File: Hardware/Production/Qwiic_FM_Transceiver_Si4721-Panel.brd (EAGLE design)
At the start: 54.6 x 34.3 mm, 60 parts, among them J1 AUDIO_JACK_3.5MM_SMD, J2 AUDIO_JACK_3.5MM_SMD, J4 QWIIC_RIGHT_ANGLE, J5 QWIIC_RIGHT_ANGLE, U1 SI4721, U3 TPA6111A2DR, Y1 32.768kHz

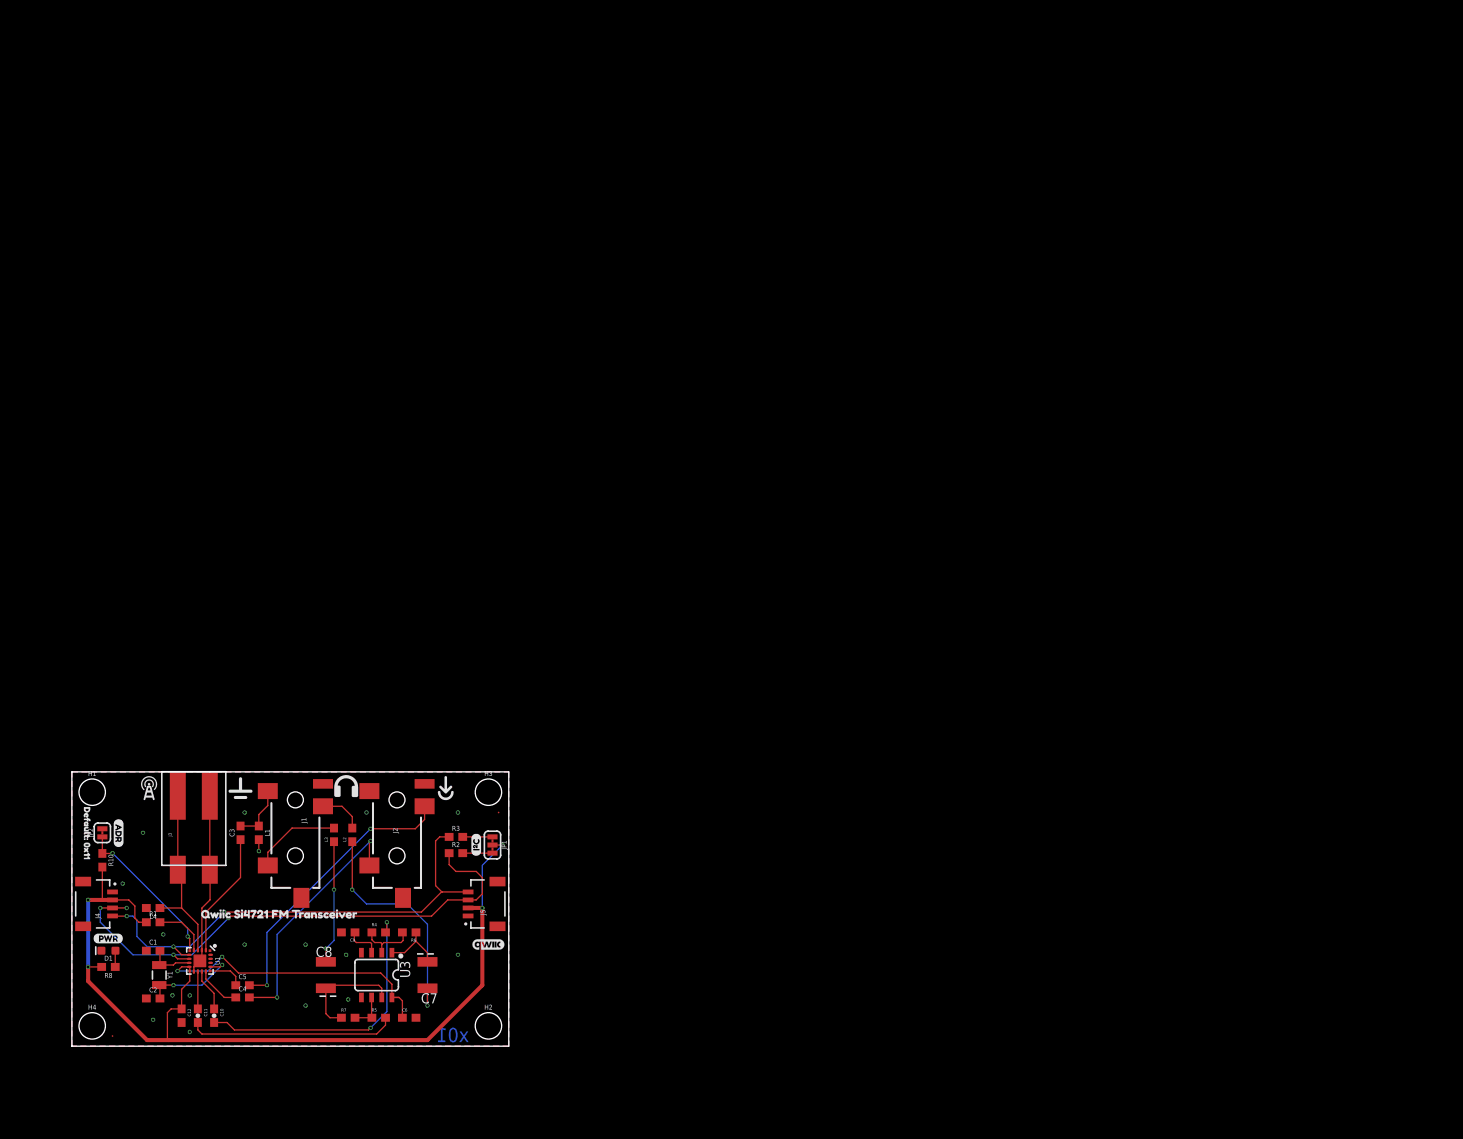
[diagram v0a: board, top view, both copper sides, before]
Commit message: x01 protos ordered
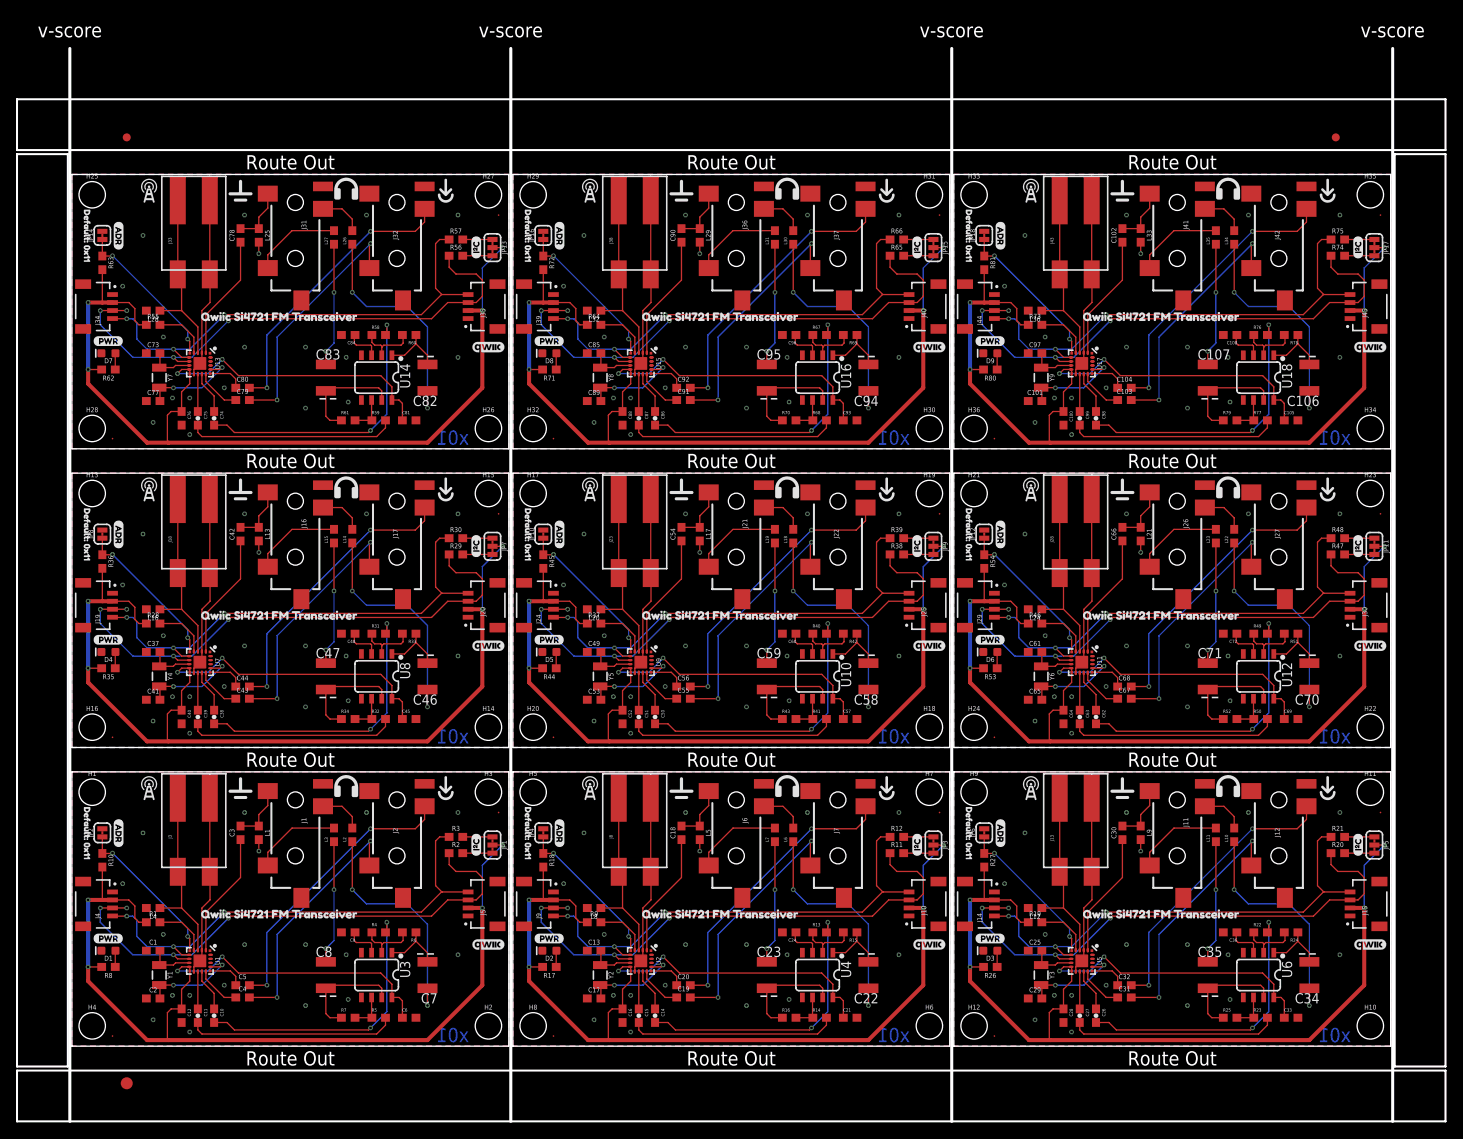
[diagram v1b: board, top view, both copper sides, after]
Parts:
- removed FRAME1: FRAME-LETTER, SparkFun-Aesthetics:CREATIVE_COMMONS
- added C100, C16, C28, C40, C52, C64, C76, C88: 22nF, SparkFun-Capacitors:0603
- added C101, C13, C17, C25, C29, C37, C41, C49, C53, C61, C65, C73, C77, C85, C89, C97: 15pF, SparkFun-Capacitors:0603
- added C102, C18, C30, C42, C54, C66, C78, C90: 1nF, SparkFun-Capacitors:0603
- added C103, C104, C19, C20, C31, C32, C43, C44, C55, C56, C67, C68, C79, C80, C91, C92: 0.47uF, SparkFun-Capacitors:0603
- added C105, C108, C21, C24, C33, C36, C45, C48, C57, C60, C69, C72, C81, C84, C93, C96: 0.1uF, SparkFun-Capacitors:0603
- added C106, C107, C22, C23, C34, C35, C46, C47, C58, C59, C70, C71, C82, C83, C94, C95: 47uF, SparkFun-Capacitors:EIA3528
- added C14, C15, C26, C27, C38, C39, C50, C51, C62, C63, C74, C75, C86, C87, C98, C99: 1uF, SparkFun-Capacitors:0603-CAP
- added D2, D3, D4, D5, D6, D7, D8, D9: RED, SparkFun-LED:LED-0603
- added E$1, E$2: (no value), SparkFun-Aesthetics:FIDUCIAL-1X2
- added E$3: (no value), SparkFun-Retired:FIDUCIAL-1.5X3
- added FD10, FD11, FD12, FD13, FD14, FD15, FD16, FD17, FD18, FD3, FD4, FD5, FD6, FD7, FD8, FD9: FIDUCIAL0.2MM, SparkFun-Aesthetics:FIDUCIAL-0.2MM
- added H10, H11, H12, H13, H14, H15, H16, H17, H18, H19, H20, H21, H22, H23, H24, H25, H26, H27, H28, H29, H30, H31, H32, H33, H34, H35, H36, H5, H6, H7, H8, H9: STAND-OFF, SparkFun-Hardware:STAND-OFF
- added J10, J14, J15, J19, J20, J24, J25, J29, J30, J34, J35, J39, J40, J44, J45, J9: QWIIC_RIGHT_ANGLE, SparkFun-Connectors:JST04_1MM_RA
- added J11, J12, J16, J17, J21, J22, J26, J27, J31, J32, J36, J37, J41, J42, J6, J7: AUDIO_JACK_3.5MM_SMD, SparkFun-Connectors:AUDIO-JACK-3.5MM-SMD
- added J13, J18, J23, J28, J33, J38, J43, J8: (no value), SparkFun-Connectors:1X02_POKEHOME
- added JP10, JP12, JP14, JP16, JP18, JP4, JP6, JP8: (no value), SparkFun-Jumpers:SMT-JUMPER_2_NC_TRACE_SILK
- added JP11, JP13, JP15, JP17, JP3, JP5, JP7, JP9: JUMPER-SMT_3_2-NC_TRACE_SILK, SparkFun-Jumpers:SMT-JUMPER_3_2-NC_TRACE_SILK
- added L10, L14, L18, L22, L26, L30, L34, L6: FERITE 2.5k, SparkFun-Coils:0603
- added L11, L15, L19, L23, L27, L31, L35, L7: FERITE 2.5K, SparkFun-Coils:0603
- added L12, L16, L20, L24, L28, L32, L36, L8: 120nH, SparkFun-Coils:0603
- added L13, L17, L21, L25, L29, L33, L5, L9: 270nH, SparkFun-Coils:0603
- added R11, R12, R20, R21, R29, R30, R38, R39, R47, R48, R56, R57, R65, R66, R74, R75: 2.2k, SparkFun-Resistors:0603
- added R13, R14, R15, R16, R22, R23, R24, R25, R31, R32, R33, R34, R40, R41, R42, R43, R49, R50, R51, R52, R58, R59, R60, R61, R67, R68, R69, R70, R76, R77, R78, R79: 20k, SparkFun-Resistors:0603
- added R17, R26, R35, R44, R53, R62, R71, R80: 1k, SparkFun-Resistors:0603
- added R18, R27, R36, R45, R54, R63, R72, R81: 100k, SparkFun-Resistors:0603
- added R19, R28, R37, R46, R55, R64, R73, R9: 10k, SparkFun-Resistors:0603
- added U$100, U$117, U$134, U$151, U$32, U$49, U$66, U$83: (no value), Labels:PWR-()-03
- added U$101, U$118, U$135, U$152, U$33, U$50, U$67, U$84: (no value), Labels:I_SUPER2_C-()-03
- added U$102, U$119, U$136, U$153, U$34, U$51, U$68, U$85: (no value), Labels:ADR-()-03
- added U$103, U$115, U$120, U$132, U$137, U$149, U$17, U$30, U$35, U$47, U$52, U$64, U$69, U$81, U$86, U$98: (no value), si4721label:QWIIC_SI4721_FM_TRANSCEIVER0
- added U$104, U$121, U$138, U$19, U$36, U$53, U$70, U$87: (no value), SparkFun-Aesthetics:QWIIC_4MM
- added U$105, U$122, U$139, U$20, U$37, U$54, U$71, U$88: (no value), SparkFun-Aesthetics:OSHW-LOGO-S
- added U$106, U$123, U$140, U$21, U$38, U$55, U$72, U$89: (no value), si4721connlabels:ANTENNA1
- added U$107, U$124, U$141, U$22, U$39, U$56, U$73, U$90: (no value), si4721connlabels:GND0
- added U$108, U$125, U$142, U$23, U$40, U$57, U$74, U$91: (no value), si4721connlabels:LINE_IN2
- added U$109, U$126, U$143, U$24, U$41, U$58, U$75, U$92: (no value), si4721connlabels:PHONES_OUT3
- added U$110, U$127, U$144, U$25, U$42, U$59, U$76, U$93: (no value), phones#png:PHONES#PNG
- added U$111, U$128, U$145, U$26, U$43, U$60, U$77, U$94: (no value), in#png:IN#PNG
- added U$112, U$129, U$146, U$27, U$44, U$61, U$78, U$95: (no value), gnd#png:GND#PNG
- added U$113, U$130, U$147, U$28, U$45, U$62, U$79, U$96: (no value), antenna#png:ANTENNA#PNG
- added U$114, U$131, U$148, U$29, U$46, U$63, U$80, U$97: SPARKX-LOGO4, SparkX:SPARKX-MEDIUM
- added U$116, U$133, U$150, U$31, U$48, U$65, U$82, U$99: (no value), defaultadr:DEFAULT#_0X110
- added U10, U12, U14, U16, U18, U4, U6, U8: TPA6111A2DR, SparkFun-IC-Amplifiers:SO08
- added U11, U13, U15, U17, U2, U5, U7, U9: SI4721, SparkFun-RF:QFN-20-3X3MM
- added Y2, Y3, Y4, Y5, Y6, Y7, Y8, Y9: 32.768kHz, SparkFun-Clocks:CRYSTAL-SMD-3.2X1.5MM
- moved J3 0.25 mm to (15.2, 27.1)
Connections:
- new net 3.3V1: C16.1, C21.1, J10.2, J9.2, JP3.2, R17.2, R18.2, R9.1, U2.10, U2.11, U4.8
- new net 3.3V2: C28.1, C33.1, J14.2, J15.2, JP5.2, R19.1, R26.2, R27.2, U5.10, U5.11, U6.8
- new net 3.3V3: C40.1, C45.1, J19.2, J20.2, JP7.2, R28.1, R35.2, R36.2, U7.10, U7.11, U8.8
- new net 3.3V4: C52.1, C57.1, J24.2, J25.2, JP9.2, R37.1, R44.2, R45.2, U10.8, U9.10, U9.11
- new net 3.3V5: C64.1, C69.1, J29.2, J30.2, JP11.2, R46.1, R53.2, R54.2, U11.10, U11.11, U12.8
- new net 3.3V6: C76.1, C81.1, J34.2, J35.2, JP13.2, R55.1, R62.2, R63.2, U13.10, U13.11, U14.8
- new net 3.3V7: C88.1, C93.1, J39.2, J40.2, JP15.2, R64.1, R71.2, R72.2, U15.10, U15.11, U16.8
- new net 3.3V8: C100.1, C105.1, J44.2, J45.2, JP17.2, R73.1, R80.2, R81.2, U17.10, U17.11, U18.8
- new net ADDR1: JP4.1, R18.1, U2.6
- new net ADDR2: JP6.1, R27.1, U5.6
- new net ADDR3: JP8.1, R36.1, U7.6
- new net ADDR4: JP10.1, R45.1, U9.6
- new net ADDR5: JP12.1, R54.1, U11.6
- new net ADDR6: JP14.1, R63.1, U13.6
- new net ADDR7: JP16.1, R72.1, U15.6
- new net ADDR8: JP18.1, R81.1, U17.6
- new net FMI1: C18.1, U2.2
- new net FMI2: C30.1, U5.2
- new net FMI3: C42.1, U7.2
- new net FMI4: C54.1, U9.2
- new net FMI5: C66.1, U11.2
- new net FMI6: C78.1, U13.2
- new net FMI7: C90.1, U15.2
- new net FMI8: C102.1, U17.2
- new net GND1: C13.1, C16.2, C17.1, C21.2, C24.2, D2.C, J10.1, J7.SLEEVE, J8.P1, J8.P3, J9.1, JP4.2, L5.2, L8.2, U2.12, U2.21, U2.3, U4.4, U4.5
- new net GND2: C25.1, C28.2, C29.1, C33.2, C36.2, D3.C, J12.SLEEVE, J13.P1, J13.P3, J14.1, J15.1, JP6.2, L12.2, L9.2, U5.12, U5.21, U5.3, U6.4, U6.5
- new net GND3: C37.1, C40.2, C41.1, C45.2, C48.2, D4.C, J17.SLEEVE, J18.P1, J18.P3, J19.1, J20.1, JP8.2, L13.2, L16.2, U7.12, U7.21, U7.3, U8.4, U8.5
- new net GND4: C49.1, C52.2, C53.1, C57.2, C60.2, D5.C, J22.SLEEVE, J23.P1, J23.P3, J24.1, J25.1, JP10.2, L17.2, L20.2, U10.4, U10.5, U9.12, U9.21, U9.3
- new net GND5: C61.1, C64.2, C65.1, C69.2, C72.2, D6.C, J27.SLEEVE, J28.P1, J28.P3, J29.1, J30.1, JP12.2, L21.2, L24.2, U11.12, U11.21, U11.3, U12.4, U12.5
- new net GND6: C73.1, C76.2, C77.1, C81.2, C84.2, D7.C, J32.SLEEVE, J33.P1, J33.P3, J34.1, J35.1, JP14.2, L25.2, L28.2, U13.12, U13.21, U13.3, U14.4, U14.5
- new net GND7: C85.1, C88.2, C89.1, C93.2, C96.2, D8.C, J37.SLEEVE, J38.P1, J38.P3, J39.1, J40.1, JP16.2, L29.2, L32.2, U15.12, U15.21, U15.3, U16.4, U16.5
- new net GND8: C100.2, C101.1, C105.2, C108.2, C97.1, D9.C, J42.SLEEVE, J43.P1, J43.P3, J44.1, J45.1, JP18.2, L33.2, L36.2, U17.12, U17.21, U17.3, U18.4, U18.5
- new net GPO10: U9.18
- new net GPO11: U11.19
- new net GPO12: U11.18
- new net GPO13: U13.19
- new net GPO14: U13.18
- new net GPO15: U15.19
- new net GPO16: U15.18
- new net GPO17: U17.19
- new net GPO18: U17.18
- new net GPO3: U2.19
- new net GPO4: U2.18
- new net GPO5: U5.19
- new net GPO6: U5.18
- new net GPO7: U7.19
- new net GPO8: U7.18
- new net GPO9: U9.19
- new net LIN1: C20.1, U2.16
- new net LIN2: C32.1, U5.16
- new net LIN3: C44.1, U7.16
- new net LIN4: C56.1, U9.16
- new net LIN5: C68.1, U11.16
- new net LIN6: C80.1, U13.16
- new net LIN7: C92.1, U15.16
- new net LIN8: C104.1, U17.16
- new net LOUT1: C14.1, U2.14
- new net LOUT2: C26.1, U5.14
- new net LOUT3: C38.1, U7.14
- new net LOUT4: C50.1, U9.14
- new net LOUT5: C62.1, U11.14
- new net LOUT6: C74.1, U13.14
- new net LOUT7: C86.1, U15.14
- new net LOUT8: C98.1, U17.14
- new net N$100: D5.A, R44.1
- new net N$101: C61.2, U11.9, Y6.P$1
- new net N$102: C65.2, U11.17, Y6.P$2
- new net N$103: R46.2, U11.5
- new net N$104: C66.2, J26.SLEEVE, L21.1
- new net N$105: C70.A, R51.1, U12.1
- new net N$106: C71.A, R52.1, U12.7
- new net N$107: C72.1, U12.3
- new net N$108: R49.1, R51.2, U12.2
- new net N$109: R50.1, R52.2, U12.6
- new net N$110: C62.2, R49.2
- new net N$111: C63.2, R50.2
- new net N$112: C70.C, L22.1
- new net N$113: C71.C, L23.1
- new net N$114: J26.RING, L22.2
- new net N$115: J26.TIP, L23.2
- new net N$116: C67.2, J27.TIP
- new net N$117: C68.2, J27.RING
- new net N$118: JP11.3, R47.2
- new net N$119: JP11.1, R48.2
- new net N$120: D6.A, R53.1
- new net N$121: C73.2, U13.9, Y7.P$1
- new net N$122: C77.2, U13.17, Y7.P$2
- new net N$123: R55.2, U13.5
- new net N$124: C78.2, J31.SLEEVE, L25.1
- new net N$125: C82.A, R60.1, U14.1
- new net N$126: C83.A, R61.1, U14.7
- new net N$127: C84.1, U14.3
- new net N$128: R58.1, R60.2, U14.2
- new net N$129: R59.1, R61.2, U14.6
- new net N$130: C74.2, R58.2
- new net N$131: C75.2, R59.2
- new net N$132: C82.C, L26.1
- new net N$133: C83.C, L27.1
- new net N$134: J31.RING, L26.2
- new net N$135: J31.TIP, L27.2
- new net N$136: C79.2, J32.TIP
- new net N$137: C80.2, J32.RING
- new net N$138: JP13.3, R56.2
- new net N$139: JP13.1, R57.2
- new net N$140: D7.A, R62.1
- new net N$141: C85.2, U15.9, Y8.P$1
- new net N$142: C89.2, U15.17, Y8.P$2
- new net N$143: R64.2, U15.5
- new net N$144: C90.2, J36.SLEEVE, L29.1
- new net N$145: C94.A, R69.1, U16.1
- new net N$146: C95.A, R70.1, U16.7
- new net N$147: C96.1, U16.3
- new net N$148: R67.1, R69.2, U16.2
- new net N$149: R68.1, R70.2, U16.6
- new net N$150: C86.2, R67.2
- new net N$151: C87.2, R68.2
- new net N$152: C94.C, L30.1
- new net N$153: C95.C, L31.1
- new net N$154: J36.RING, L30.2
- new net N$155: J36.TIP, L31.2
- new net N$156: C91.2, J37.TIP
- new net N$157: C92.2, J37.RING
- new net N$158: JP15.3, R65.2
- new net N$159: JP15.1, R66.2
- new net N$160: D8.A, R71.1
- new net N$161: C97.2, U17.9, Y9.P$1
- new net N$162: C101.2, U17.17, Y9.P$2
- new net N$163: R73.2, U17.5
- new net N$164: C102.2, J41.SLEEVE, L33.1
- new net N$165: C106.A, R78.1, U18.1
- new net N$166: C107.A, R79.1, U18.7
- new net N$167: C108.1, U18.3
- new net N$168: R76.1, R78.2, U18.2
- new net N$169: R77.1, R79.2, U18.6
- new net N$170: C98.2, R76.2
- new net N$171: C99.2, R77.2
- new net N$172: C106.C, L34.1
- new net N$173: C107.C, L35.1
- new net N$174: J41.RING, L34.2
- new net N$175: J41.TIP, L35.2
- new net N$176: C103.2, J42.TIP
- new net N$177: C104.2, J42.RING
- new net N$178: JP17.3, R74.2
- new net N$179: JP17.1, R75.2
- new net N$180: D9.A, R80.1
- new net N$21: C13.2, U2.9, Y2.P$1
- new net N$22: C17.2, U2.17, Y2.P$2
- new net N$23: R9.2, U2.5
- new net N$24: C18.2, J6.SLEEVE, L5.1
- new net N$25: C22.A, R15.1, U4.1
- new net N$26: C23.A, R16.1, U4.7
- new net N$27: C24.1, U4.3
- new net N$28: R13.1, R15.2, U4.2
- new net N$29: R14.1, R16.2, U4.6
- new net N$30: C14.2, R13.2
- new net N$31: C15.2, R14.2
- new net N$32: C22.C, L6.1
- new net N$33: C23.C, L7.1
- new net N$34: J6.RING, L6.2
- new net N$35: J6.TIP, L7.2
- new net N$36: C19.2, J7.TIP
- new net N$37: C20.2, J7.RING
- new net N$38: JP3.3, R11.2
- new net N$39: JP3.1, R12.2
- new net N$40: D2.A, R17.1
- new net N$41: C25.2, U5.9, Y3.P$1
- new net N$42: C29.2, U5.17, Y3.P$2
- new net N$43: R19.2, U5.5
- new net N$44: C30.2, J11.SLEEVE, L9.1
- new net N$45: C34.A, R24.1, U6.1
- new net N$46: C35.A, R25.1, U6.7
- new net N$47: C36.1, U6.3
- new net N$48: R22.1, R24.2, U6.2
- new net N$49: R23.1, R25.2, U6.6
- new net N$50: C26.2, R22.2
- new net N$51: C27.2, R23.2
- new net N$52: C34.C, L10.1
- new net N$53: C35.C, L11.1
- new net N$54: J11.RING, L10.2
- new net N$55: J11.TIP, L11.2
- new net N$56: C31.2, J12.TIP
- new net N$57: C32.2, J12.RING
- new net N$58: JP5.3, R20.2
- new net N$59: JP5.1, R21.2
- new net N$60: D3.A, R26.1
- new net N$61: C37.2, U7.9, Y4.P$1
- new net N$62: C41.2, U7.17, Y4.P$2
- new net N$63: R28.2, U7.5
- new net N$64: C42.2, J16.SLEEVE, L13.1
- new net N$65: C46.A, R33.1, U8.1
- new net N$66: C47.A, R34.1, U8.7
- new net N$67: C48.1, U8.3
- new net N$68: R31.1, R33.2, U8.2
- new net N$69: R32.1, R34.2, U8.6
- new net N$70: C38.2, R31.2
- new net N$71: C39.2, R32.2
- new net N$72: C46.C, L14.1
- new net N$73: C47.C, L15.1
- new net N$74: J16.RING, L14.2
- new net N$75: J16.TIP, L15.2
- new net N$76: C43.2, J17.TIP
- new net N$77: C44.2, J17.RING
- new net N$78: JP7.3, R29.2
- new net N$79: JP7.1, R30.2
- new net N$80: D4.A, R35.1
- new net N$81: C49.2, U9.9, Y5.P$1
- new net N$82: C53.2, U9.17, Y5.P$2
- new net N$83: R37.2, U9.5
- new net N$84: C54.2, J21.SLEEVE, L17.1
- new net N$85: C58.A, R42.1, U10.1
- new net N$86: C59.A, R43.1, U10.7
- new net N$87: C60.1, U10.3
- new net N$88: R40.1, R42.2, U10.2
- new net N$89: R41.1, R43.2, U10.6
- new net N$90: C50.2, R40.2
- new net N$91: C51.2, R41.2
- new net N$92: C58.C, L18.1
- new net N$93: C59.C, L19.1
- new net N$94: J21.RING, L18.2
- new net N$95: J21.TIP, L19.2
- new net N$96: C55.2, J22.TIP
- new net N$97: C56.2, J22.RING
- new net N$98: JP9.3, R38.2
- new net N$99: JP9.1, R39.2
- new net RIN1: C19.1, U2.15
- new net RIN2: C31.1, U5.15
- new net RIN3: C43.1, U7.15
- new net RIN4: C55.1, U9.15
- new net RIN5: C67.1, U11.15
- new net RIN6: C79.1, U13.15
- new net RIN7: C91.1, U15.15
- new net RIN8: C103.1, U17.15
- new net ROUT1: C15.1, U2.13
- new net ROUT2: C27.1, U5.13
- new net ROUT3: C39.1, U7.13
- new net ROUT4: C51.1, U9.13
- new net ROUT5: C63.1, U11.13
- new net ROUT6: C75.1, U13.13
- new net ROUT7: C87.1, U15.13
- new net ROUT8: C99.1, U17.13
- new net SCLK1: J10.4, J9.4, R12.1, U2.7
- new net SCLK2: J14.4, J15.4, R21.1, U5.7
- new net SCLK3: J19.4, J20.4, R30.1, U7.7
- new net SCLK4: J24.4, J25.4, R39.1, U9.7
- new net SCLK5: J29.4, J30.4, R48.1, U11.7
- new net SCLK6: J34.4, J35.4, R57.1, U13.7
- new net SCLK7: J39.4, J40.4, R66.1, U15.7
- new net SCLK8: J44.4, J45.4, R75.1, U17.7
- new net SDIO1: J10.3, J9.3, R11.1, U2.8
- new net SDIO2: J14.3, J15.3, R20.1, U5.8
- new net SDIO3: J19.3, J20.3, R29.1, U7.8
- new net SDIO4: J24.3, J25.3, R38.1, U9.8
- new net SDIO5: J29.3, J30.3, R47.1, U11.8
- new net SDIO6: J34.3, J35.3, R56.1, U13.8
- new net SDIO7: J39.3, J40.3, R65.1, U15.8
- new net SDIO8: J44.3, J45.3, R74.1, U17.8
- new net TXO1: J8.P2, J8.P4, L8.1, U2.4
- new net TXO2: J13.P2, J13.P4, L12.1, U5.4
- new net TXO3: J18.P2, J18.P4, L16.1, U7.4
- new net TXO4: J23.P2, J23.P4, L20.1, U9.4
- new net TXO5: J28.P2, J28.P4, L24.1, U11.4
- new net TXO6: J33.P2, J33.P4, L28.1, U13.4
- new net TXO7: J38.P2, J38.P4, L32.1, U15.4
- new net TXO8: J43.P2, J43.P4, L36.1, U17.4
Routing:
- net 3.3V4: track 0.00 -> 149.1 mm, vias 0 -> 6
- net 3.3V3: track 0.00 -> 149.1 mm, vias 0 -> 6
- net 3.3V8: track 0.00 -> 149.1 mm, vias 0 -> 6
- net 3.3V5: track 0.00 -> 149.1 mm, vias 0 -> 6
- net 3.3V2: track 0.00 -> 149.1 mm, vias 0 -> 6
- net 3.3V7: track 0.00 -> 149.1 mm, vias 0 -> 6
- net 3.3V6: track 0.00 -> 149.1 mm, vias 0 -> 6
- net 3.3V1: track 0.00 -> 149.1 mm, vias 0 -> 6
- net SDIO8: track 0.00 -> 68.1 mm, vias 0 -> 4
- net SDIO5: track 0.00 -> 68.1 mm, vias 0 -> 4
- net SDIO2: track 0.00 -> 68.1 mm, vias 0 -> 4
- net SDIO7: track 0.00 -> 68.1 mm, vias 0 -> 4
- net SDIO4: track 0.00 -> 68.1 mm, vias 0 -> 4
- net SDIO3: track 0.00 -> 68.1 mm, vias 0 -> 4
- net SDIO1: track 0.00 -> 68.1 mm, vias 0 -> 4
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- added copper zone on layer 1, net GND1
- added copper zone on layer 16, net GND1
- added copper zone on layer 1, net GND2
- added copper zone on layer 16, net GND2
- added copper zone on layer 1, net GND3
- added copper zone on layer 16, net GND3
- added copper zone on layer 1, net GND4
- added copper zone on layer 16, net GND4
- added copper zone on layer 1, net GND5
- added copper zone on layer 16, net GND5
- added copper zone on layer 1, net GND6
- added copper zone on layer 16, net GND6
- added copper zone on layer 1, net GND7
- added copper zone on layer 16, net GND7
- added copper zone on layer 1, net GND8
- added copper zone on layer 16, net GND8
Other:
- board size 54.6 x 34.3 mm -> 178.6 x 134.1 mm
- board text added: "Route Out"
- board text added: "v-score"

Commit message: x02 hardware order
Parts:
- removed C100, C88: 22nF, SparkFun-Capacitors:0603
- removed C101, C85, C89, C97: 15pF, SparkFun-Capacitors:0603
- removed C102, C90: 1nF, SparkFun-Capacitors:0603
- removed C103, C104, C79, C80, C91, C92: 0.47uF, SparkFun-Capacitors:0603
- removed C105, C108, C81, C84, C93, C96: 0.1uF, SparkFun-Capacitors:0603
- removed C106, C107, C82, C83, C94, C95: 47uF, SparkFun-Capacitors:EIA3528
- removed C86, C87, C98, C99: 1uF, SparkFun-Capacitors:0603-CAP
- removed D7, D8, D9: RED, SparkFun-LED:LED-0603
- removed FD13, FD14, FD15, FD16, FD17, FD18: FIDUCIAL0.2MM, SparkFun-Aesthetics:FIDUCIAL-0.2MM
- removed H25, H26, H27, H28, H29, H30, H31, H32, H33, H34, H35, H36: STAND-OFF, SparkFun-Hardware:STAND-OFF
- removed J31, J32, J36, J37, J41, J42: AUDIO_JACK_3.5MM_SMD, SparkFun-Connectors:AUDIO-JACK-3.5MM-SMD
- removed J33, J38, J43: (no value), SparkFun-Connectors:1X02_POKEHOME
- removed J34, J35, J39, J40, J44, J45: QWIIC_RIGHT_ANGLE, SparkFun-Connectors:JST04_1MM_RA
- removed JP13, JP15, JP17: JUMPER-SMT_3_2-NC_TRACE_SILK, SparkFun-Jumpers:SMT-JUMPER_3_2-NC_TRACE_SILK
- removed JP14, JP16, JP18: (no value), SparkFun-Jumpers:SMT-JUMPER_2_NC_TRACE_SILK
- removed L25, L29, L33: 270nH, SparkFun-Coils:0603
- removed L26, L30, L34: FERITE 2.5k, SparkFun-Coils:0603
- removed L27, L31, L35: FERITE 2.5K, SparkFun-Coils:0603
- removed L28, L32, L36: 120nH, SparkFun-Coils:0603
- removed R55, R64, R73: 10k, SparkFun-Resistors:0603
- removed R56, R57, R65, R66, R74, R75: 2.2k, SparkFun-Resistors:0603
- removed R58, R59, R60, R61, R67, R68, R69, R70, R76, R77, R78, R79: 20k, SparkFun-Resistors:0603
- removed R62, R71, R80: 1k, SparkFun-Resistors:0603
- removed R63, R72, R81: 100k, SparkFun-Resistors:0603
- removed U$109, U$126, U$143: (no value), si4721connlabels:PHONES_OUT3
- removed U$110, U$127, U$144: (no value), phones#png:PHONES#PNG
- removed U$111, U$128, U$145: (no value), in#png:IN#PNG
- removed U$112, U$129, U$146: (no value), gnd#png:GND#PNG
- removed U$113, U$130, U$147: (no value), antenna#png:ANTENNA#PNG
- removed U$114, U$131, U$148: SPARKX-LOGO4, SparkX:SPARKX-MEDIUM
- removed U$115, U$120, U$132, U$137, U$149: (no value), si4721label:QWIIC_SI4721_FM_TRANSCEIVER0
- removed U$116, U$133, U$150: (no value), defaultadr:DEFAULT#_0X110
- removed U$117, U$134, U$151: (no value), Labels:PWR-()-03
- removed U$118, U$135, U$152: (no value), Labels:I_SUPER2_C-()-03
- removed U$119, U$136, U$153: (no value), Labels:ADR-()-03
- removed U$121, U$138: (no value), SparkFun-Aesthetics:QWIIC_4MM
- removed U$122, U$139: (no value), SparkFun-Aesthetics:OSHW-LOGO-S
- removed U$123, U$140: (no value), si4721connlabels:ANTENNA1
- removed U$124, U$141: (no value), si4721connlabels:GND0
- removed U$125, U$142: (no value), si4721connlabels:LINE_IN2
- removed U13, U15, U17: SI4721, SparkFun-RF:QFN-20-3X3MM
- removed U14, U16, U18: TPA6111A2DR, SparkFun-IC-Amplifiers:SO08
- removed Y7, Y8, Y9: 32.768kHz, SparkFun-Clocks:CRYSTAL-SMD-3.2X1.5MM
- C13, C65: value 15pF -> 2.2uF
- C14, C27: value 1uF -> 15pF; device SparkFun-Capacitors:0603-CAP -> SparkFun-Capacitors:0603
- C16, C28: value 22nF -> 1uF; device SparkFun-Capacitors:0603 -> SparkFun-Capacitors:0603-CAP
- C17: value 15pF -> 22nF
- C18, C66: value 1nF -> 15pF
- C19, C32: value 0.47uF -> 1nF
- C21, C33, C60, C72: value 0.1uF -> 0.47uF
- C22, C35: value 47uF -> 0.1uF; device SparkFun-Capacitors:EIA3528 -> SparkFun-Capacitors:0603
- C24, C36: value 0.1uF -> 47uF; device SparkFun-Capacitors:0603 -> SparkFun-Capacitors:EIA3528
- C25, C61, C77: value 15pF -> 0.1uF
- C26, C39: value 1uF -> 2.2uF; device SparkFun-Capacitors:0603-CAP -> SparkFun-Capacitors:0603
- C29, C41: value 15pF -> 1uF; device SparkFun-Capacitors:0603 -> SparkFun-Capacitors:0603-CAP
- C30: value 1nF -> 22nF
- C31, C44: value 0.47uF -> 15pF
- C34, C46, C47, C59: value 47uF -> 0.47uF; device SparkFun-Capacitors:EIA3528 -> SparkFun-Capacitors:0603
- C37, C49: value 15pF -> 47uF; device SparkFun-Capacitors:0603 -> SparkFun-Capacitors:EIA3528
- C38, C51, C74: value 1uF -> 0.1uF; device SparkFun-Capacitors:0603-CAP -> SparkFun-Capacitors:0603
- C40: value 22nF -> 15pF
- C42, C54: value 1nF -> 1uF; device SparkFun-Capacitors:0603 -> SparkFun-Capacitors:0603-CAP
- C43, C56: value 0.47uF -> 22nF
- C45: value 0.1uF -> 1nF
- C50, C62, C63, C75: value 1uF -> 47uF; device SparkFun-Capacitors:0603-CAP -> SparkFun-Capacitors:EIA3528
- C52: value 22nF -> 2.2uF
- C55, C67, C68: value 0.47uF -> 1uF; device SparkFun-Capacitors:0603 -> SparkFun-Capacitors:0603-CAP
- C57: value 0.1uF -> 15pF
- C58, C71: value 47uF -> 1nF; device SparkFun-Capacitors:EIA3528 -> SparkFun-Capacitors:0603
- C64: value 22nF -> 0.1uF
- C69: value 0.1uF -> 22nF
- C70: value 47uF -> 15pF; device SparkFun-Capacitors:EIA3528 -> SparkFun-Capacitors:0603
- C73: value 15pF -> 0.47uF
- C76: value 22nF -> 47uF; device SparkFun-Capacitors:0603 -> SparkFun-Capacitors:EIA3528
- C78: value 1nF -> 2.2uF
- U$100: device Labels:PWR-()-03 -> gnd#png:GND#PNG
- U$101: device Labels:I_SUPER2_C-()-03 -> antenna#png:ANTENNA#PNG
- U$102: value (none) -> SPARKX-LOGO4; device Labels:ADR-()-03 -> SparkX:SPARKX-MEDIUM
- U$104: device SparkFun-Aesthetics:QWIIC_4MM -> Labels:PWR-()-03
- U$105: device SparkFun-Aesthetics:OSHW-LOGO-S -> Labels:I_SUPER2_C-()-03
- U$106: device si4721connlabels:ANTENNA1 -> Labels:ADR-()-03
- U$107: device si4721connlabels:GND0 -> addr_labels:CLOSED_0X110
- U$108: device si4721connlabels:LINE_IN2 -> addr_labels:OPEN_0X631
- U$15: device defaultadr:DEFAULT#_0X110 -> addr_labels:CLOSED_0X110
- U$17: device si4721label:QWIIC_SI4721_FM_TRANSCEIVER0 -> addr_labels:OPEN_0X631
- U$19: device SparkFun-Aesthetics:QWIIC_4MM -> si4721label:QWIIC_SI4721_FM_TRANSCEIVER0
- U$20: device SparkFun-Aesthetics:OSHW-LOGO-S -> SparkFun-Aesthetics:QWIIC_4MM
- U$21: device si4721connlabels:ANTENNA1 -> SparkFun-Aesthetics:OSHW-LOGO-S
- U$22: device si4721connlabels:GND0 -> si4721connlabels:ANTENNA1
- U$23: device si4721connlabels:LINE_IN2 -> si4721connlabels:GND0
- U$24: device si4721connlabels:PHONES_OUT3 -> si4721connlabels:LINE_IN2
- U$25: device phones#png:PHONES#PNG -> si4721connlabels:PHONES_OUT3
- U$26: device in#png:IN#PNG -> phones#png:PHONES#PNG
- U$27: device gnd#png:GND#PNG -> in#png:IN#PNG
- U$28: device antenna#png:ANTENNA#PNG -> gnd#png:GND#PNG
- U$29: value SPARKX-LOGO4 -> (none); device SparkX:SPARKX-MEDIUM -> antenna#png:ANTENNA#PNG
- U$30: value (none) -> SPARKX-LOGO4; device si4721label:QWIIC_SI4721_FM_TRANSCEIVER0 -> SparkX:SPARKX-MEDIUM
- U$31: device defaultadr:DEFAULT#_0X110 -> si4721label:QWIIC_SI4721_FM_TRANSCEIVER0
- U$35: device si4721label:QWIIC_SI4721_FM_TRANSCEIVER0 -> addr_labels:CLOSED_0X110
- U$36: device SparkFun-Aesthetics:QWIIC_4MM -> addr_labels:OPEN_0X631
- U$37: device SparkFun-Aesthetics:OSHW-LOGO-S -> si4721label:QWIIC_SI4721_FM_TRANSCEIVER0
- U$38: device si4721connlabels:ANTENNA1 -> SparkFun-Aesthetics:QWIIC_4MM
- U$39: device si4721connlabels:GND0 -> SparkFun-Aesthetics:OSHW-LOGO-S
- U$40: device si4721connlabels:LINE_IN2 -> si4721connlabels:ANTENNA1
- U$41: device si4721connlabels:PHONES_OUT3 -> si4721connlabels:GND0
- U$42: device phones#png:PHONES#PNG -> si4721connlabels:LINE_IN2
- U$43: device in#png:IN#PNG -> si4721connlabels:PHONES_OUT3
- U$44: device gnd#png:GND#PNG -> phones#png:PHONES#PNG
- U$45: device antenna#png:ANTENNA#PNG -> in#png:IN#PNG
- U$46: value SPARKX-LOGO4 -> (none); device SparkX:SPARKX-MEDIUM -> gnd#png:GND#PNG
- U$47: device si4721label:QWIIC_SI4721_FM_TRANSCEIVER0 -> antenna#png:ANTENNA#PNG
- U$48: value (none) -> SPARKX-LOGO4; device defaultadr:DEFAULT#_0X110 -> SparkX:SPARKX-MEDIUM
- U$49: device Labels:PWR-()-03 -> si4721label:QWIIC_SI4721_FM_TRANSCEIVER0
- U$50: device Labels:I_SUPER2_C-()-03 -> Labels:PWR-()-03
- U$51: device Labels:ADR-()-03 -> Labels:I_SUPER2_C-()-03
- U$52: device si4721label:QWIIC_SI4721_FM_TRANSCEIVER0 -> Labels:ADR-()-03
- U$53: device SparkFun-Aesthetics:QWIIC_4MM -> addr_labels:CLOSED_0X110
- U$54: device SparkFun-Aesthetics:OSHW-LOGO-S -> addr_labels:OPEN_0X631
- U$55: device si4721connlabels:ANTENNA1 -> si4721label:QWIIC_SI4721_FM_TRANSCEIVER0
- U$56: device si4721connlabels:GND0 -> SparkFun-Aesthetics:QWIIC_4MM
- U$57: device si4721connlabels:LINE_IN2 -> SparkFun-Aesthetics:OSHW-LOGO-S
- U$58: device si4721connlabels:PHONES_OUT3 -> si4721connlabels:ANTENNA1
- U$59: device phones#png:PHONES#PNG -> si4721connlabels:GND0
- U$60: device in#png:IN#PNG -> si4721connlabels:LINE_IN2
- U$61: device gnd#png:GND#PNG -> si4721connlabels:PHONES_OUT3
- U$62: device antenna#png:ANTENNA#PNG -> phones#png:PHONES#PNG
- U$63: value SPARKX-LOGO4 -> (none); device SparkX:SPARKX-MEDIUM -> in#png:IN#PNG
- U$64: device si4721label:QWIIC_SI4721_FM_TRANSCEIVER0 -> gnd#png:GND#PNG
- U$65: device defaultadr:DEFAULT#_0X110 -> antenna#png:ANTENNA#PNG
- U$66: value (none) -> SPARKX-LOGO4; device Labels:PWR-()-03 -> SparkX:SPARKX-MEDIUM
- U$67: device Labels:I_SUPER2_C-()-03 -> si4721label:QWIIC_SI4721_FM_TRANSCEIVER0
- U$68: device Labels:ADR-()-03 -> Labels:PWR-()-03
- U$69: device si4721label:QWIIC_SI4721_FM_TRANSCEIVER0 -> Labels:I_SUPER2_C-()-03
- U$70: device SparkFun-Aesthetics:QWIIC_4MM -> Labels:ADR-()-03
- U$71: device SparkFun-Aesthetics:OSHW-LOGO-S -> addr_labels:CLOSED_0X110
- U$72: device si4721connlabels:ANTENNA1 -> addr_labels:OPEN_0X631
- U$73: device si4721connlabels:GND0 -> si4721label:QWIIC_SI4721_FM_TRANSCEIVER0
- U$74: device si4721connlabels:LINE_IN2 -> SparkFun-Aesthetics:QWIIC_4MM
- U$75: device si4721connlabels:PHONES_OUT3 -> SparkFun-Aesthetics:OSHW-LOGO-S
- U$76: device phones#png:PHONES#PNG -> si4721connlabels:ANTENNA1
- U$77: device in#png:IN#PNG -> si4721connlabels:GND0
- U$78: device gnd#png:GND#PNG -> si4721connlabels:LINE_IN2
- U$79: device antenna#png:ANTENNA#PNG -> si4721connlabels:PHONES_OUT3
- U$80: value SPARKX-LOGO4 -> (none); device SparkX:SPARKX-MEDIUM -> phones#png:PHONES#PNG
- U$81: device si4721label:QWIIC_SI4721_FM_TRANSCEIVER0 -> in#png:IN#PNG
- U$82: device defaultadr:DEFAULT#_0X110 -> gnd#png:GND#PNG
- U$83: device Labels:PWR-()-03 -> antenna#png:ANTENNA#PNG
- U$84: value (none) -> SPARKX-LOGO4; device Labels:I_SUPER2_C-()-03 -> SparkX:SPARKX-MEDIUM
- U$85: device Labels:ADR-()-03 -> si4721label:QWIIC_SI4721_FM_TRANSCEIVER0
- U$86: device si4721label:QWIIC_SI4721_FM_TRANSCEIVER0 -> Labels:PWR-()-03
- U$87: device SparkFun-Aesthetics:QWIIC_4MM -> Labels:I_SUPER2_C-()-03
- U$88: device SparkFun-Aesthetics:OSHW-LOGO-S -> Labels:ADR-()-03
- U$89: device si4721connlabels:ANTENNA1 -> addr_labels:CLOSED_0X110
- U$90: device si4721connlabels:GND0 -> addr_labels:OPEN_0X631
- U$91: device si4721connlabels:LINE_IN2 -> si4721label:QWIIC_SI4721_FM_TRANSCEIVER0
- U$92: device si4721connlabels:PHONES_OUT3 -> SparkFun-Aesthetics:QWIIC_4MM
- U$93: device phones#png:PHONES#PNG -> SparkFun-Aesthetics:OSHW-LOGO-S
- U$94: device in#png:IN#PNG -> si4721connlabels:ANTENNA1
- U$95: device gnd#png:GND#PNG -> si4721connlabels:GND0
- U$96: device antenna#png:ANTENNA#PNG -> si4721connlabels:LINE_IN2
- U$97: value SPARKX-LOGO4 -> (none); device SparkX:SPARKX-MEDIUM -> si4721connlabels:PHONES_OUT3
- U$98: device si4721label:QWIIC_SI4721_FM_TRANSCEIVER0 -> phones#png:PHONES#PNG
- U$99: device defaultadr:DEFAULT#_0X110 -> in#png:IN#PNG
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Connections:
- removed net 3.3V6: C76.1, C81.1, J34.2, J35.2, JP13.2, R55.1, R62.2, R63.2, U13.10, U13.11, U14.8
- removed net 3.3V7: C88.1, C93.1, J39.2, J40.2, JP15.2, R64.1, R71.2, R72.2, U15.10, U15.11, U16.8
- removed net 3.3V8: C100.1, C105.1, J44.2, J45.2, JP17.2, R73.1, R80.2, R81.2, U17.10, U17.11, U18.8
- removed net ADDR6: JP14.1, R63.1, U13.6
- removed net ADDR7: JP16.1, R72.1, U15.6
- removed net ADDR8: JP18.1, R81.1, U17.6
- removed net FMI6: C78.1, U13.2
- removed net FMI7: C90.1, U15.2
- removed net FMI8: C102.1, U17.2
- removed net GND6: C73.1, C76.2, C77.1, C81.2, C84.2, D7.C, J32.SLEEVE, J33.P1, J33.P3, J34.1, J35.1, JP14.2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
- removed net GND7: C85.1, C88.2, C89.1, C93.2, C96.2, D8.C, J37.SLEEVE, J38.P1, J38.P3, J39.1, J40.1, JP16.2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
- removed net GND8: C100.2, C101.1, C105.2, C108.2, C97.1, D9.C, J42.SLEEVE, J43.P1, J43.P3, J44.1, J45.1, JP18.2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
- removed net GPO13: U13.19
- removed net GPO14: U13.18
- removed net GPO15: U15.19
- removed net GPO16: U15.18
- removed net GPO17: U17.19
- removed net GPO18: U17.18
- removed net LIN6: C80.1, U13.16
- removed net LIN7: C92.1, U15.16
- removed net LIN8: C104.1, U17.16
- removed net LOUT6: C74.1, U13.14
- removed net LOUT7: C86.1, U15.14
- removed net LOUT8: C98.1, U17.14
- removed net N$121: C73.2, U13.9, Y7.P$1
- removed net N$122: C77.2, U13.17, Y7.P$2
- removed net N$123: R55.2, U13.5
- removed net N$124: C78.2, J31.SLEEVE, L25.1
- removed net N$125: C82.A, R60.1, U14.1
- removed net N$126: C83.A, R61.1, U14.7
- removed net N$127: C84.1, U14.3
- removed net N$128: R58.1, R60.2, U14.2
- removed net N$129: R59.1, R61.2, U14.6
- removed net N$130: C74.2, R58.2
- removed net N$131: C75.2, R59.2
- removed net N$132: C82.C, L26.1
- removed net N$133: C83.C, L27.1
- removed net N$134: J31.RING, L26.2
- removed net N$135: J31.TIP, L27.2
- removed net N$136: C79.2, J32.TIP
- removed net N$137: C80.2, J32.RING
- removed net N$138: JP13.3, R56.2
- removed net N$139: JP13.1, R57.2
- removed net N$140: D7.A, R62.1
- removed net N$141: C85.2, U15.9, Y8.P$1
- removed net N$142: C89.2, U15.17, Y8.P$2
- removed net N$143: R64.2, U15.5
- removed net N$144: C90.2, J36.SLEEVE, L29.1
- removed net N$145: C94.A, R69.1, U16.1
- removed net N$146: C95.A, R70.1, U16.7
- removed net N$147: C96.1, U16.3
- removed net N$148: R67.1, R69.2, U16.2
- removed net N$149: R68.1, R70.2, U16.6
- removed net N$150: C86.2, R67.2
- removed net N$151: C87.2, R68.2
- removed net N$152: C94.C, L30.1
- removed net N$153: C95.C, L31.1
- removed net N$154: J36.RING, L30.2
- removed net N$155: J36.TIP, L31.2
- removed net N$156: C91.2, J37.TIP
- removed net N$157: C92.2, J37.RING
- removed net N$158: JP15.3, R65.2
- removed net N$159: JP15.1, R66.2
- removed net N$160: D8.A, R71.1
- removed net N$161: C97.2, U17.9, Y9.P$1
- removed net N$162: C101.2, U17.17, Y9.P$2
- removed net N$163: R73.2, U17.5
- removed net N$164: C102.2, J41.SLEEVE, L33.1
- removed net N$165: C106.A, R78.1, U18.1
- removed net N$166: C107.A, R79.1, U18.7
- removed net N$167: C108.1, U18.3
- removed net N$168: R76.1, R78.2, U18.2
- removed net N$169: R77.1, R79.2, U18.6
- removed net N$170: C98.2, R76.2
- removed net N$171: C99.2, R77.2
- removed net N$172: C106.C, L34.1
- removed net N$173: C107.C, L35.1
- removed net N$174: J41.RING, L34.2
- removed net N$175: J41.TIP, L35.2
- removed net N$176: C103.2, J42.TIP
- removed net N$177: C104.2, J42.RING
- removed net N$178: JP17.3, R74.2
- removed net N$179: JP17.1, R75.2
- removed net N$180: D9.A, R80.1
- removed net RIN6: C79.1, U13.15
- removed net RIN7: C91.1, U15.15
- removed net RIN8: C103.1, U17.15
- removed net ROUT6: C75.1, U13.13
- removed net ROUT7: C87.1, U15.13
- removed net ROUT8: C99.1, U17.13
- removed net SCLK6: J34.4, J35.4, R57.1, U13.7
- removed net SCLK7: J39.4, J40.4, R66.1, U15.7
- removed net SCLK8: J44.4, J45.4, R75.1, U17.7
- removed net SDIO6: J34.3, J35.3, R56.1, U13.8
- removed net SDIO7: J39.3, J40.3, R65.1, U15.8
- removed net SDIO8: J44.3, J45.3, R74.1, U17.8
- removed net TXO6: J33.P2, J33.P4, L28.1, U13.4
- removed net TXO7: J38.P2, J38.P4, L32.1, U15.4
- removed net TXO8: J43.P2, J43.P4, L36.1, U17.4
- net 3.3V1: now also C17.1, C22.1; no longer C16.1, C21.1
- net 3.3V2: now also C30.1, C35.1; no longer C28.1, C33.1
- net 3.3V3: now also C43.1, C48.1; no longer C40.1, C45.1
- net 3.3V4: now also C56.1, C61.1; no longer C52.1, C57.1
- net 3.3V5: now also C74.1; no longer C64.1
- net FMI1: now also C19.1; no longer C18.1
- net FMI2: now also C32.1; no longer C30.1
- net FMI3: now also C45.1; no longer C42.1
- net FMI4: now also C58.1; no longer C54.1
- net FMI5: now also C71.1; no longer C66.1
- net GND: now also C13.2
- net GND1: now also C14.1, C17.2, C18.1, C22.2, C25.2, C26.2; no longer C13.1, C16.2, C17.1, C21.2, C24.2
- net GND2: now also C27.1, C30.2, C31.1, C35.2, C38.2, C39.2; no longer C25.1, C28.2, C29.1, C33.2, C36.2
- net GND3: now also C40.1, C43.2, C44.1, C51.2, C52.2; no longer C37.1, C40.2, C41.1, C45.2
- net GND4: now also C56.2, C57.1, C61.2, C64.2, C65.2; no longer C49.1, C52.2, C57.2, C60.2
- net GND5: now also C66.1, C70.1, C74.2, C77.2, C78.2; no longer C61.1, C64.2, C65.1, C72.2
- net LIN1: now also C21.1; no longer C20.1
- net LIN2: now also C34.1; no longer C32.1
- net LIN3: now also C47.1; no longer C44.1
- net LIN4: now also C60.1; no longer C56.1
- net LIN5: now also C73.1; no longer C68.1
- net LOUT1: now also C15.1; no longer C14.1
- net LOUT2: now also C28.1; no longer C26.1
- net LOUT3: now also C41.1; no longer C38.1
- net LOUT4: now also C54.1; no longer C50.1
- net LOUT5: now also C67.1; no longer C62.1
- net N$1: now also C13.1
- net N$101: now also C66.2; no longer C61.2
- net N$102: now also C70.2; no longer C65.2
- net N$103: now also C78.1
- net N$104: now also C71.2; no longer C66.2
- net N$105: now also C75.A; no longer C70.A
- net N$106: now also C76.A; no longer C71.A
- net N$107: now also C77.1; no longer C72.1
- net N$110: now also C67.2; no longer C62.2
- net N$111: now also C68.2; no longer C63.2
- net N$112: now also C75.C; no longer C70.C
- net N$113: now also C76.C; no longer C71.C
- net N$116: now also C72.2; no longer C67.2
- net N$117: now also C73.2; no longer C68.2
- net N$21: now also C14.2; no longer C13.2
- net N$22: now also C18.2; no longer C17.2
- net N$23: now also C26.1
- net N$24: now also C19.2; no longer C18.2
- net N$25: now also C23.A; no longer C22.A
- net N$26: now also C24.A; no longer C23.A
- net N$27: now also C25.1; no longer C24.1
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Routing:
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- removed copper zone on layer 1, net GND6
- removed copper zone on layer 16, net GND6
- removed copper zone on layer 1, net GND7
- removed copper zone on layer 16, net GND7
- removed copper zone on layer 1, net GND8
- removed copper zone on layer 16, net GND8
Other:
- board size 178.6 x 134.1 mm -> 123.4 x 134.1 mm
- board text added: "What Size Antenna Should You Use? ------------------------- ½ wave FM whip antenna ≌ 160cm ¼ wave FM whip antenna ≌ 80cm (practically, for desktop testing purposes, jamming any piece of wire in there will work)"
- board text added: "x02"
- board text removed: "x01"
